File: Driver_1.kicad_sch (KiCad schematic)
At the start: 32 parts

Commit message: VER2.2: все изменения в списке изменений
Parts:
- D31, D32: value NSI6651ASC-DSWR -> ~; Description P/N (none) -> Gate driver; Product Name (none) -> NSI6651ASC-DSWR
- D33, D34: value MMSZ5240B -> ~; Description P/N (none) -> Zener diode; Product Name (none) -> MMSZ5240B
- D35, D36: value MMSZ5232B -> ~; Description P/N (none) -> Zener diode; Product Name (none) -> MMSZ5232B
- D58, D59: value MURS160 -> ~; Description P/N (none) -> Ultrafast diode; Product Name (none) -> MURS160

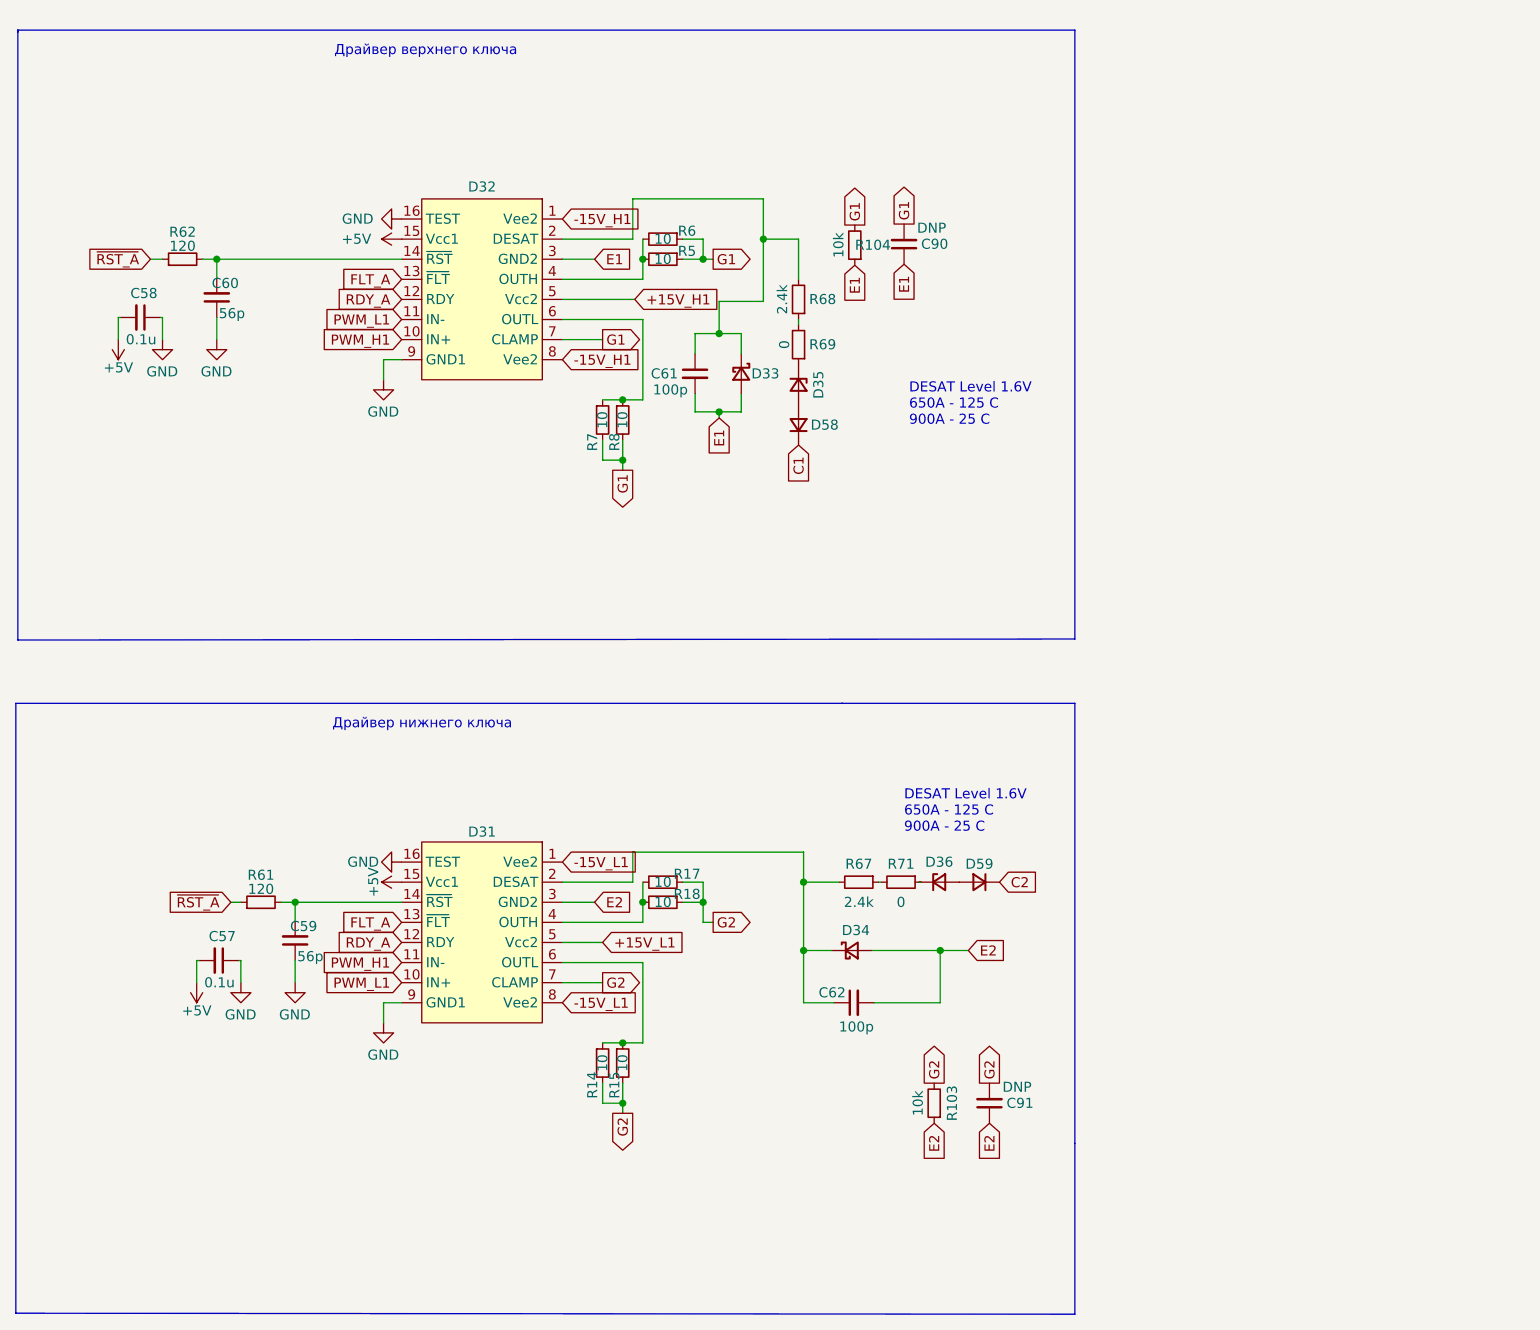
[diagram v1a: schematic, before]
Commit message: VER2.2: добавил фильтры на вход ШИМа и обновил все доки
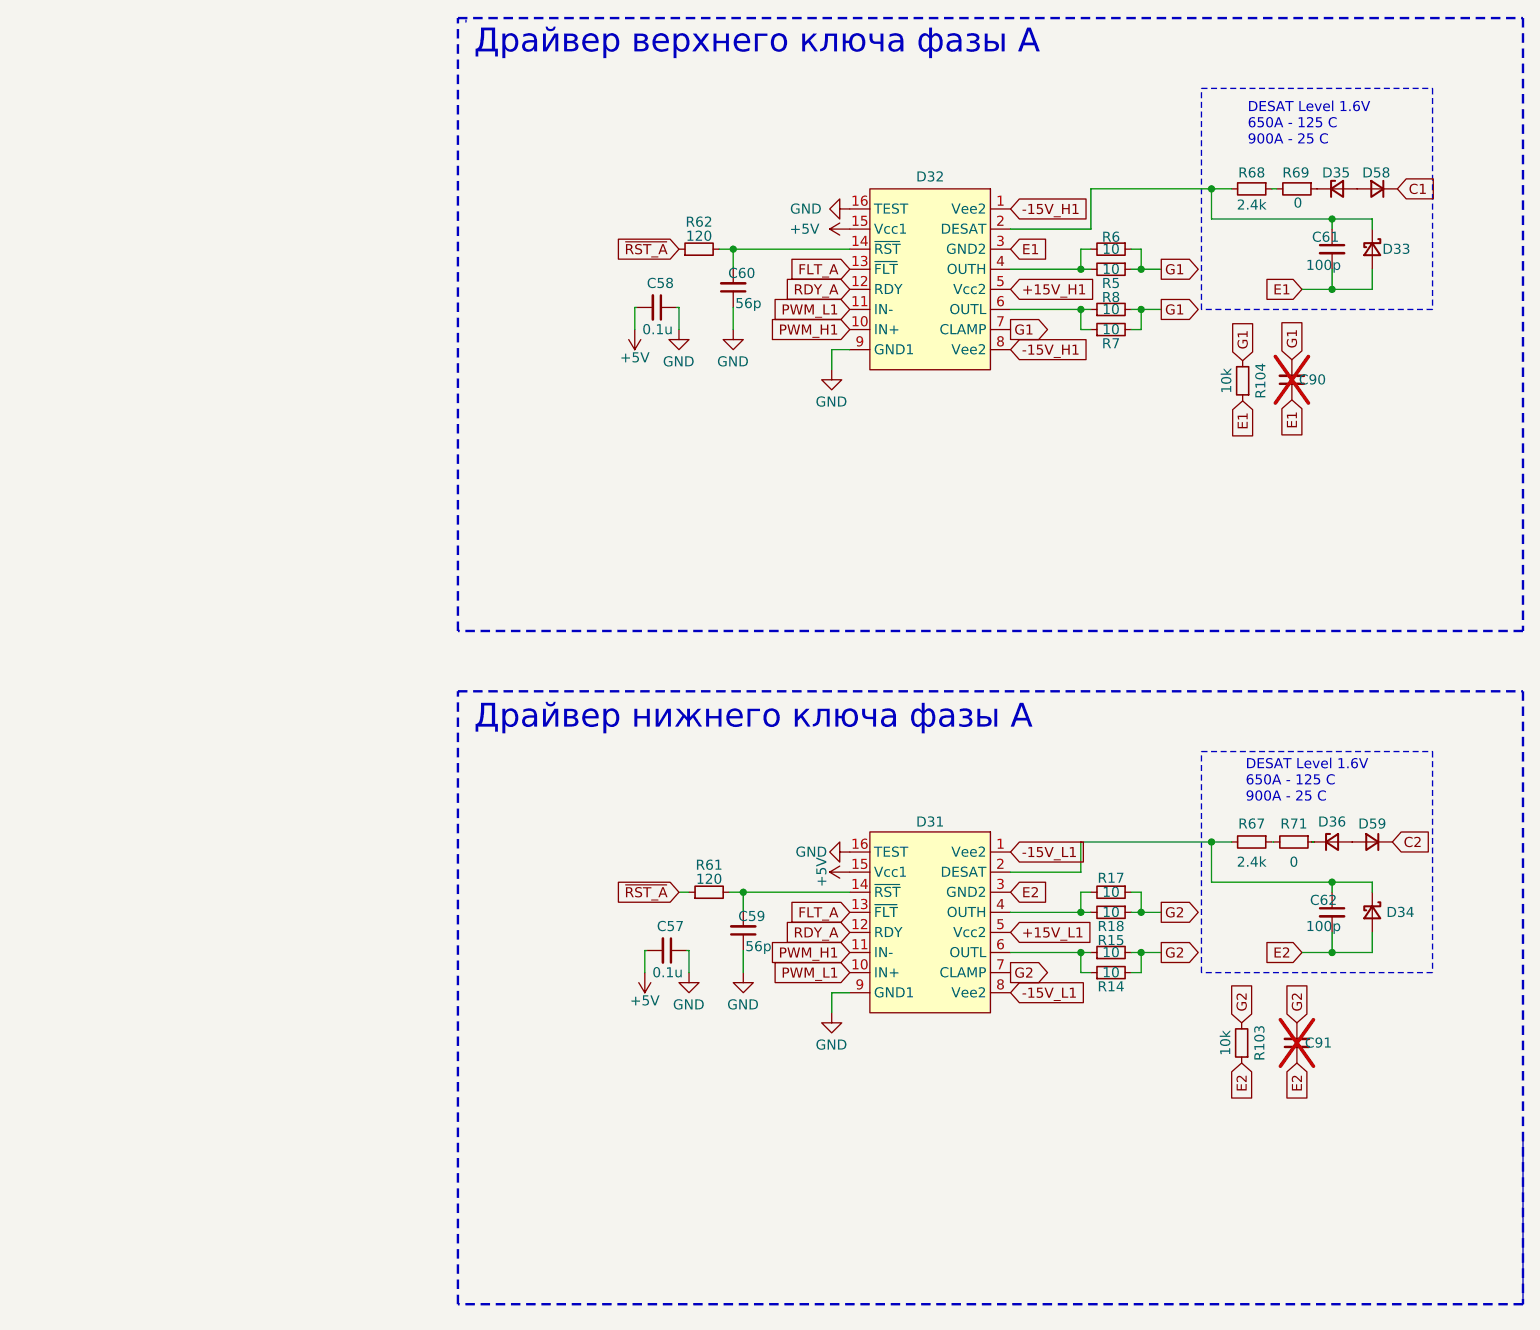
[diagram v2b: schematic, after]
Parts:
- C90, C91: value DNP -> ~; now not fitted
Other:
- note added: "Драйвер верхнего ключа фазы А"
- note added: "Драйвер нижнего ключа фазы А"
- note removed: "Драйвер верхнего ключа"
- note removed: "Драйвер нижнего ключа"
- company: (none) -> ООО "ЭТТ"
- moved on the sheet: C57, C58, C59, C60, C61, C62, D31, D32, D33, D34, D35, D36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

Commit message: VER2.2.1: исправил косяк с питанием NTC, изменил номиналы затворов и цепи NTC
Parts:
- R17, R18, R5, R6: value 10 -> 6.8
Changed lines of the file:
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@@
 			)
 		)
-		(property "Value" "10"
+		(property "Value" "6.8"
 			(at 169.672 50.8 90)
 			(effects
@@
 			)
 		)
-		(property "Value" "10"
+		(property "Value" "6.8"
 			(at 169.672 132.08 90)
 			(effects
@@
 			)
 		)
-		(property "Value" "10"
+		(property "Value" "6.8"
 			(at 169.672 53.34 90)
 			(effects
@@
 			)
 		)
-		(property "Value" "10"
+		(property "Value" "6.8"
 			(at 169.672 134.62 90)
 			(effects

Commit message: VER2.2.1: создал папку для производственных доков
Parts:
- C57, C58, C59, C60, C61, C62, C90, C91: Description P/N (none) -> Capacitor SMD 25+V
- R103, R104, R14, R15, R17, R18, R5, R6, R61, R62, R67, R68, R69, R7, R71, R8: Description P/N (none) -> Resistor SMD
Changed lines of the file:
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@@
 			)
 		)
-		(property "Description P/N" ""
+		(property "Description P/N" "Resistor SMD"
 			(at 186.309 67.437 0)
 			(effects
@@
 			)
 		)
-		(property "Description P/N" ""
+		(property "Description P/N" "Resistor SMD"
 			(at 118.872 132.08 0)
 			(effects
@@
 			)
 		)
-		(property "Description P/N" ""
+		(property "Description P/N" "Resistor SMD"
 			(at 192.786 125.73 0)
 			(effects
@@
 			)
 		)
-		(property "Description P/N" ""
+		(property "Description P/N" "Resistor SMD"
 			(at 169.672 50.8 0)
 			(effects
@@
 			)
 		)
-		(property "Description P/N" ""
+		(property "Description P/N" "Resistor SMD"
 			(at 187.452 125.73 0)
 			(effects
@@
 			)
 		)
-		(property "Description P/N" ""
+		(property "Description P/N" "Resistor SMD"
 			(at 169.672 60.96 0)
 			(effects
@@
 			)
 		)
-		(property "Description P/N" ""
+		(property "Description P/N" "Capacitor SMD 25+V"
 			(at 113.538 139.446 0)
 			(effects
@@
 			)
 		)
-		(property "Description P/N" ""
+		(property "Description P/N" "Resistor SMD"
 			(at 169.672 132.08 0)
 			(effects
@@
 			)
 		)
-		(property "Description P/N" ""
+		(property "Description P/N" "Resistor SMD"
 			(at 169.672 139.7 0)
 			(effects
@@
 			)
 		)
-		(property "Description P/N" ""
+		(property "Description P/N" "Resistor SMD"
 			(at 186.182 151.13 0)
 			(effects
@@
 			)
 		)
-		(property "Description P/N" ""
+		(property "Description P/N" "Capacitor SMD 25+V"
 			(at 112.268 58.166 0)
 			(effects
@@
 			)
 		)
-		(property "Description P/N" ""
+		(property "Description P/N" "Capacitor SMD 25+V"
 			(at 193.167 151.13 0)
 			(effects
@@
 			)
 		)
-		(property "Description P/N" ""
+		(property "Description P/N" "Resistor SMD"
 			(at 193.167 43.18 0)
 			(effects
@@
 			)
 		)
-		(property "Description P/N" ""
+		(property "Description P/N" "Resistor SMD"
 			(at 169.672 53.34 0)
 			(effects
@@
 			)
 		)
-		(property "Description P/N" ""
+		(property "Description P/N" "Capacitor SMD 25+V"
 			(at 197.612 134.62 0)
 			(effects
@@
 			)
 		)
-		(property "Description P/N" ""
+		(property "Description P/N" "Capacitor SMD 25+V"
 			(at 123.19 136.906 0)
 			(effects
@@
 			)
 		)
-		(property "Description P/N" ""
+		(property "Description P/N" "Capacitor SMD 25+V"
 			(at 192.532 67.31 0)
 			(effects
@@
 			)
 		)
-		(property "Description P/N" ""
+		(property "Description P/N" "Resistor SMD"
 			(at 117.602 50.8 0)
 			(effects
@@
 			)
 		)
-		(property "Description P/N" ""
+		(property "Description P/N" "Resistor SMD"
 			(at 187.452 43.18 0)
 			(effects
@@
 			)
 		)
-		(property "Description P/N" ""
+		(property "Description P/N" "Resistor SMD"
 			(at 169.672 58.42 0)
 			(effects
@@
 			)
 		)
-		(property "Description P/N" ""
+		(property "Description P/N" "Capacitor SMD 25+V"
 			(at 121.92 55.626 0)
 			(effects
@@
 			)
 		)
-		(property "Description P/N" ""
+		(property "Description P/N" "Capacitor SMD 25+V"
 			(at 197.612 50.8 0)
 			(effects
@@
 			)
 		)
-		(property "Description P/N" ""
+		(property "Description P/N" "Resistor SMD"
 			(at 169.672 134.62 0)
 			(effects
@@
 			)
 		)
-		(property "Description P/N" ""
+		(property "Description P/N" "Resistor SMD"
 			(at 169.672 142.24 0)
 			(effects
